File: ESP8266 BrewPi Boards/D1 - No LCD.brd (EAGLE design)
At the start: 44.9 x 34 mm, 7 parts, among them J1 RJ45-8X

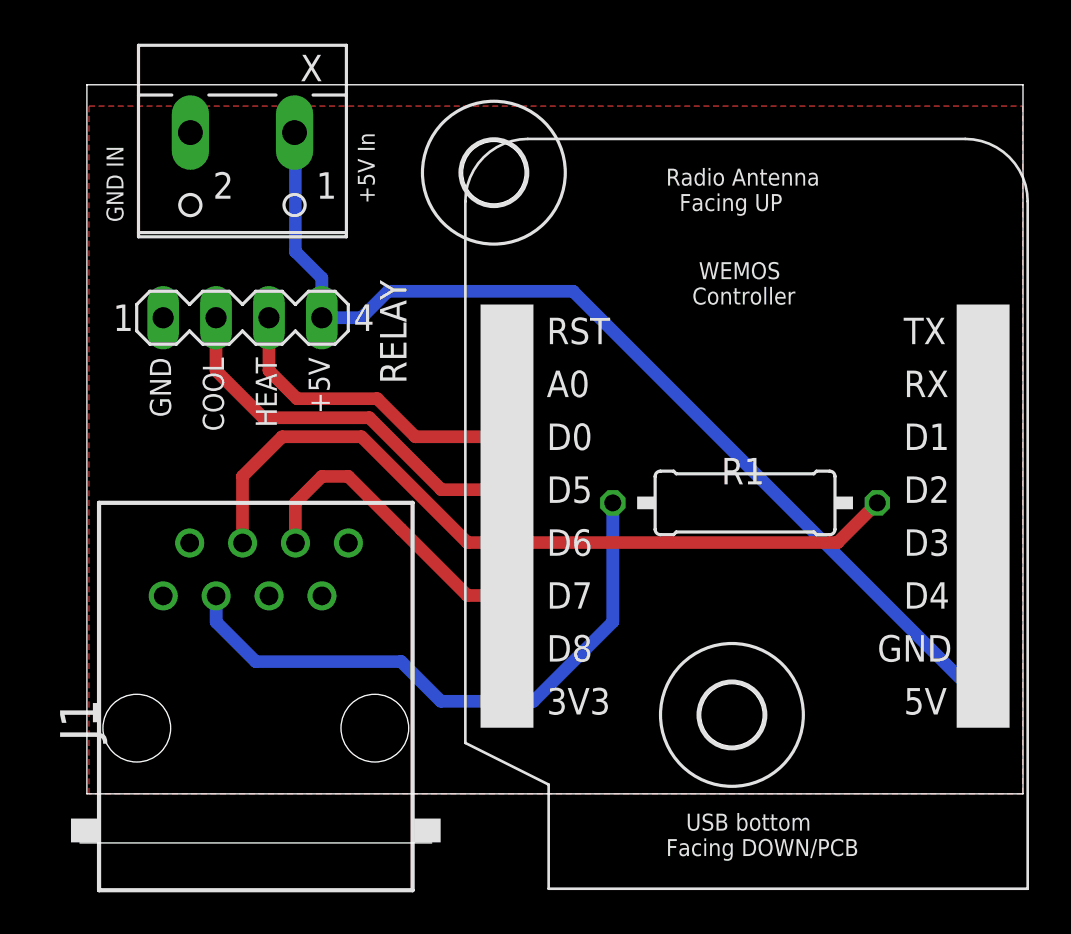
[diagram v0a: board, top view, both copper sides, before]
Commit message: Updating No LCD Boards
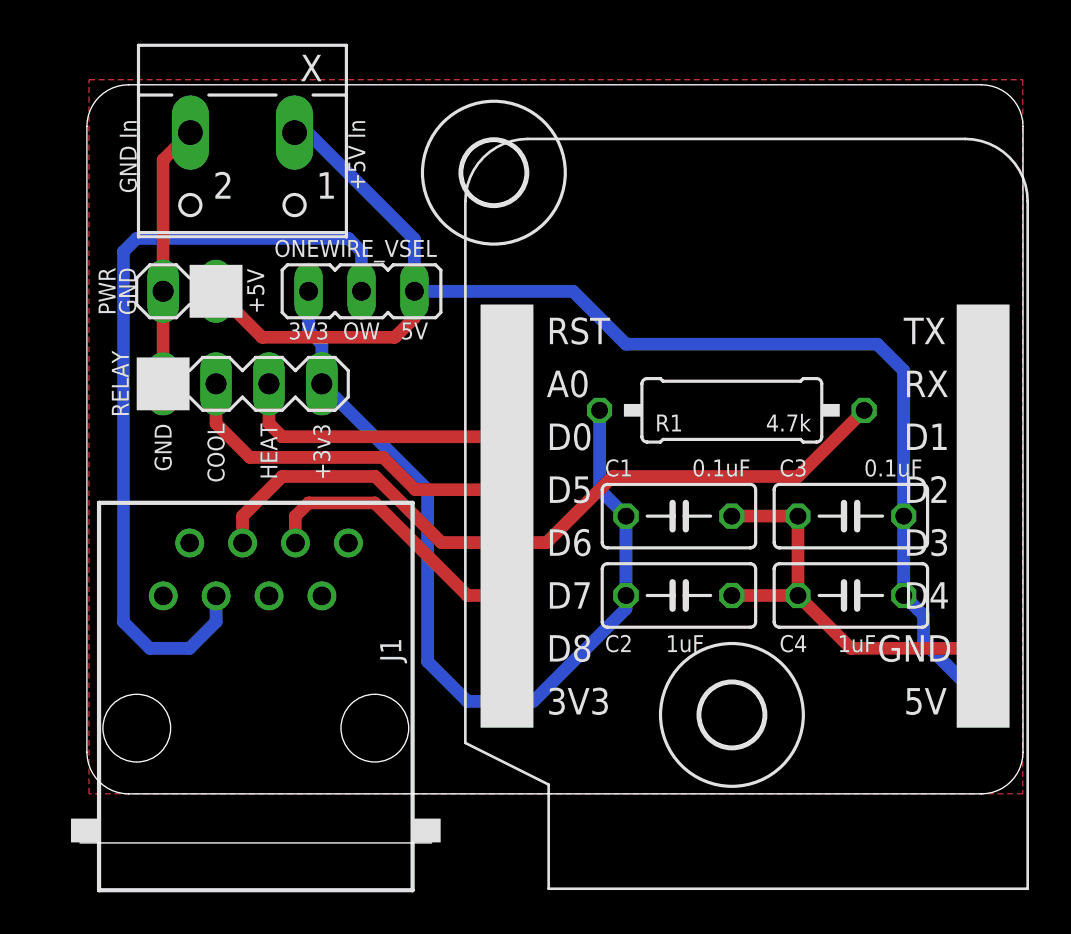
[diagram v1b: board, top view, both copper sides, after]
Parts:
- added C1, C3: 0.1uF, rcl:C050-030X075
- added C2, C4: 1uF, rcl:C050-030X075
- added ONEWIRE_VSEL: (no value), Donnie:JP2-NOLABEL
- added PWR: HDR-2, Donnie:HDR-2_VERT
- RELAY: value (none) -> HDR-4; device con-lstb:MA04-1 -> Donnie:HDR-4_VERT
- U$1: value WEMOS -> D1_MINI; device 1455413453956-wemos:WEMOS -> 1455413453956-wemos:WEMOS-CLEAN
- moved RELAY 4.96 mm to (3.81, 19.7)
- moved R1 4.49 mm to (31.1, 18.4)
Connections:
- new net N$1: J1.3, ONEWIRE_VSEL.2
- net 3V3: now also C1.1, C2.1, ONEWIRE_VSEL.3, RELAY.4; no longer J1.3
- net 5V: now also C3.1, C4.1, ONEWIRE_VSEL.1, PWR.1; no longer RELAY.4
- net GND: now also C1.2, C2.2, C3.2, C4.2, PWR.2
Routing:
- net N$1: track 0.00 -> 38.4 mm
- net GND: track 0.00 -> 32.7 mm
- net 5V: track 49.9 -> 65.1 mm
- net 3V3: track 29.2 -> 42.4 mm
- net HEAT: track 15.3 -> 13.6 mm
- net COOL: track 18.9 -> 17.2 mm
- net ONEWIRE: track 37.4 -> 35.9 mm
- net DOOR: track 15.0 -> 13.6 mm
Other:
- outline, holes or cut-outs redrawn
- board text added: "+3v3"
- board text added: "0.1uF"
- board text added: "1uF"
- board text added: "3V3"
- board text added: "4.7k"
- board text added: "5V"
- board text added: "BrewPi D1 Mini No LCD - v1.1 @thorrak says hi"
- board text added: "GND In"
- board text added: "OW"
- board text removed: "BrewPi D1 Mini No LCD - v0.2 @thorrak says hi"
- board text removed: "GND IN"

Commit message: Updating board designs and adding DirtyPCB Links
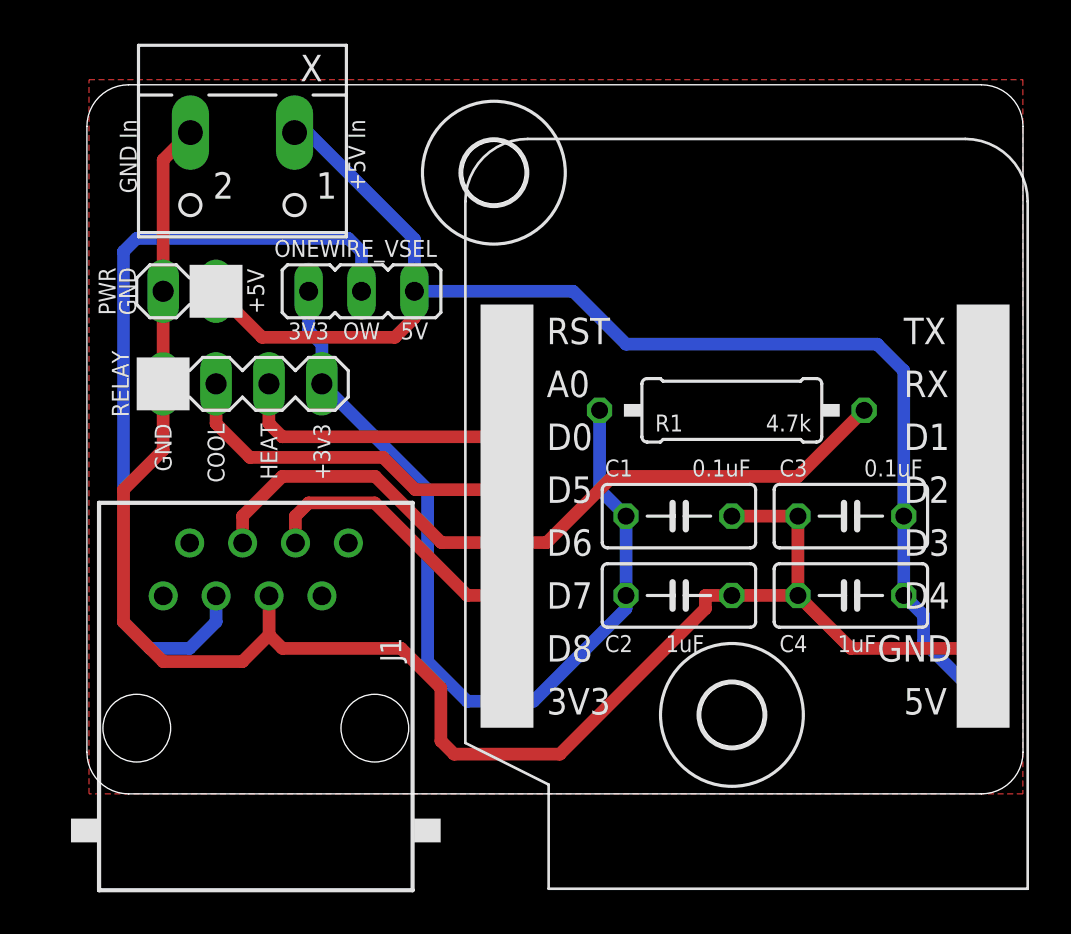
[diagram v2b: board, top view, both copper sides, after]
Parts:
- J1: device con-tycoelectronics:RJ45-NO-SHIELD -> Donnie:RJ45-NS-XDIM
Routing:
- net GND: track 32.7 -> 84.7 mm
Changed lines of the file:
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@@
 <attribute name="VALUE" x="5.12" y="24.765" size="1.27" layer="27" ratio="10"/>
 </element>
-<element name="J1" library="con-tycoelectronics" library_urn="urn:adsk.eagle:library:193" package="RJ45-NO-SHIELD" package3d_urn="urn:adsk.eagle:package:10660/1" value="RJ45-8X" x="8.26" y="3.155" smashed="yes">
+<element name="J1" library="Donnie" package="RJ45-NS-XDIM" package3d_urn="urn:adsk.eagle:package:10660/1" value="RJ45-8X" x="8.26" y="3.155" smashed="yes">
 <attribute name="MF" value="" x="8.26" y="3.155" size="1.778" layer="27" display="off"/>
 <attribute name="MPN" value="RJ45-8X" x="8.26" y="3.155" size="1.778" layer="27" display="off"/>
@@
 <wire x1="3.81" y1="30.44" x2="5.12" y2="31.75" width="0.6096" layer="1"/>
 <wire x1="3.81" y1="19.685" x2="3.81" y2="24.13" width="0.6096" layer="1"/>
-<wire x1="8.895" y1="9.505" x2="31.115" y2="9.525" width="0" layer="19" extent="1-1"/>
-<wire x1="3.81" y1="19.685" x2="8.895" y2="9.505" width="0" layer="19" extent="1-1"/>
+<wire x1="3.81" y1="19.685" x2="3.81" y2="16.51" width="0.6096" layer="1"/>
+<wire x1="3.81" y1="16.51" x2="1.905" y2="14.605" width="0.6096" layer="1"/>
+<wire x1="1.905" y1="14.605" x2="1.905" y2="8.255" width="0.6096" layer="1"/>
+<wire x1="1.905" y1="8.255" x2="3.81" y2="6.35" width="0.6096" layer="1"/>
+<wire x1="3.81" y1="6.35" x2="7.62" y2="6.35" width="0.6096" layer="1"/>
+<wire x1="8.895" y1="9.505" x2="8.895" y2="7.625" width="0.6096" layer="1"/>
+<wire x1="7.62" y1="6.35" x2="8.895" y2="7.625" width="0.6096" layer="1"/>
+<wire x1="8.895" y1="7.625" x2="9.535" y2="6.985" width="0.6096" layer="1"/>
+<wire x1="9.535" y1="6.985" x2="15.24" y2="6.985" width="0.6096" layer="1"/>
+<wire x1="15.24" y1="6.985" x2="17.145" y2="5.08" width="0.6096" layer="1"/>
+<wire x1="17.145" y1="5.08" x2="17.145" y2="2.54" width="0.6096" layer="1"/>
+<wire x1="17.145" y1="2.54" x2="17.78" y2="1.905" width="0.6096" layer="1"/>
+<wire x1="17.78" y1="1.905" x2="22.86" y2="1.905" width="0.6096" layer="1"/>
+<wire x1="22.86" y1="1.905" x2="29.845" y2="8.89" width="0.6096" layer="1"/>
+<wire x1="29.845" y1="8.89" x2="29.845" y2="9.525" width="0.6096" layer="1"/>
+<wire x1="29.845" y1="9.525" x2="31.115" y2="9.525" width="0.6096" layer="1"/>
 </signal>
 <signal name="5V" class="1">
